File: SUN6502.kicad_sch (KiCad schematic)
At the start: 52 parts, among them J1 Barrel_Jack_MountingPin, J2 6-5530843-5, J3 6-5530843-5, J4 DE9_Socket, SW1 RESET, SW2 Power Switch, U1 W65C02SxP, U10 MAX232, U11 74LS00, U2 KM62256CLP, U3 28C256, U4 W65C22NxP, U5 74LS139, U6 74LS21, U7 W65C22NxP, U8 W65C51NxP, U9 74LS138, Y1 1Mhz, Y2 1.8432Mhz

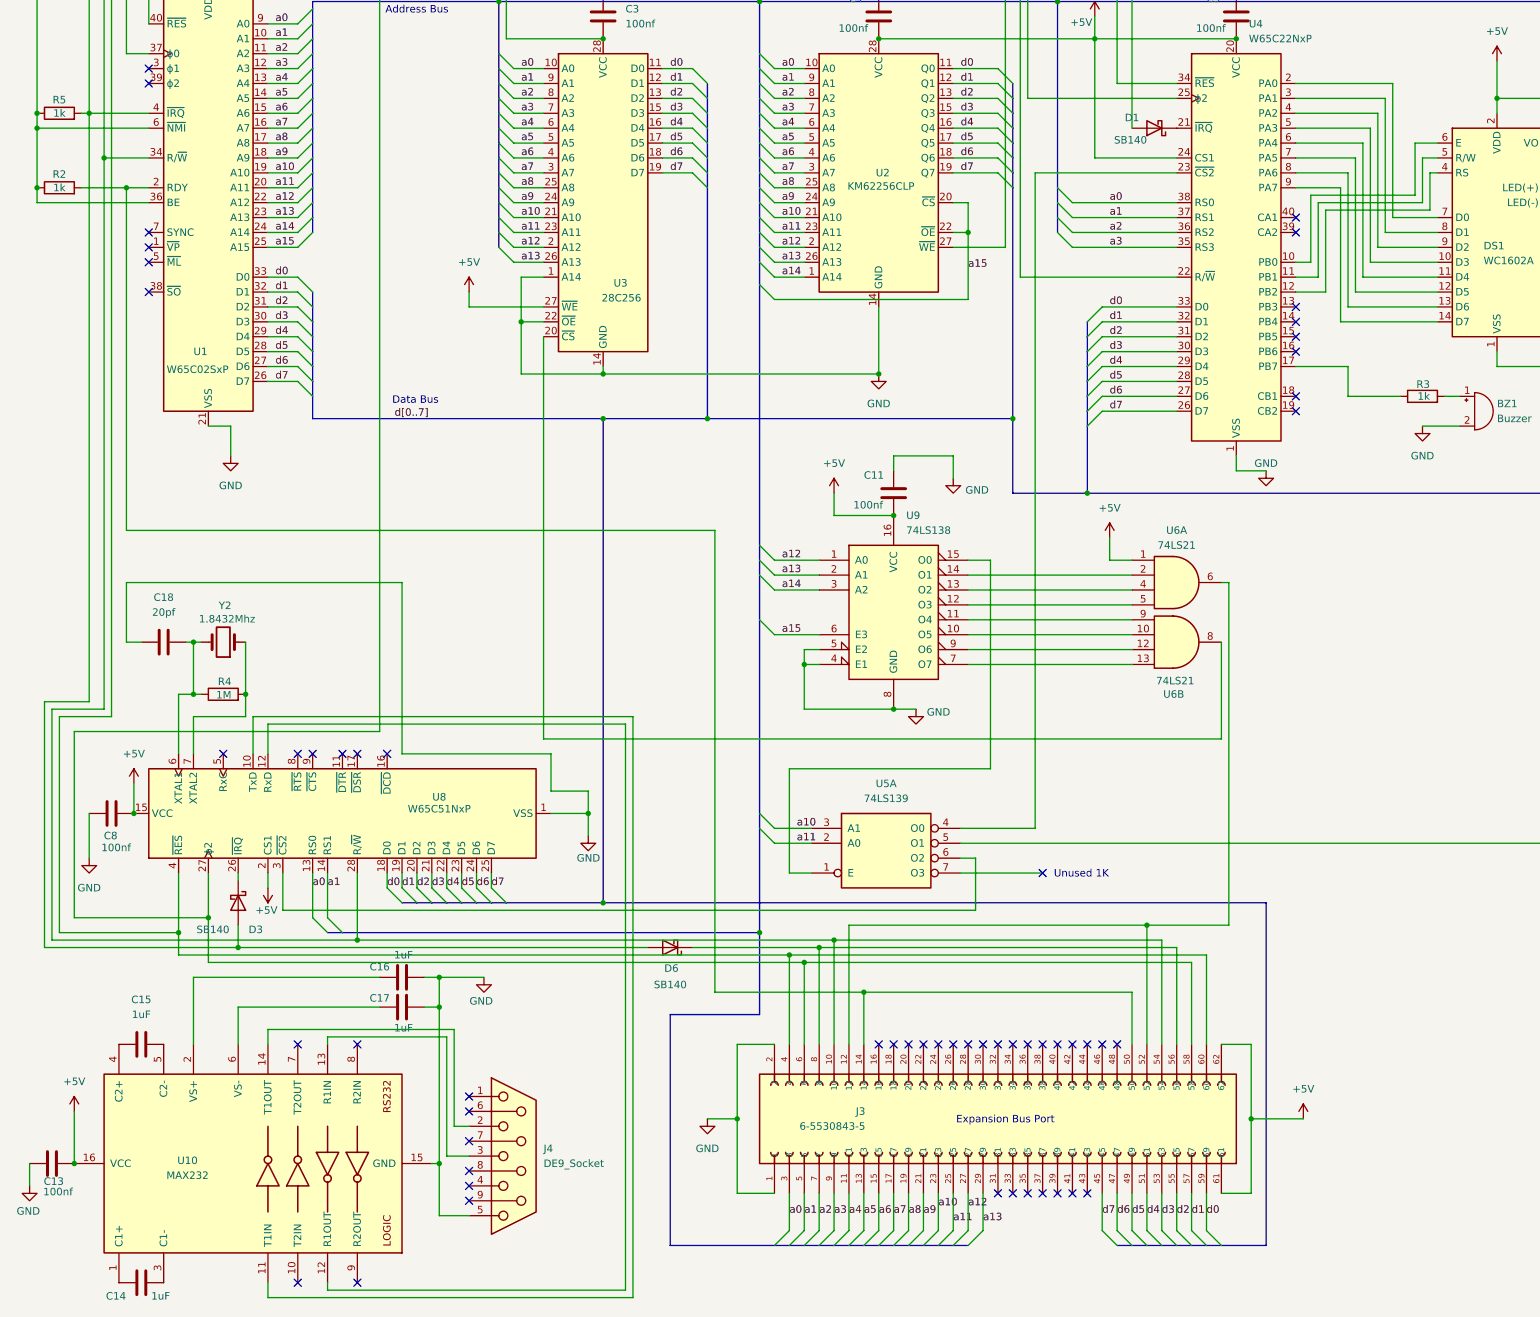
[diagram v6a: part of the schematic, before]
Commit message: pcb changed to 2 layers, CTR Added
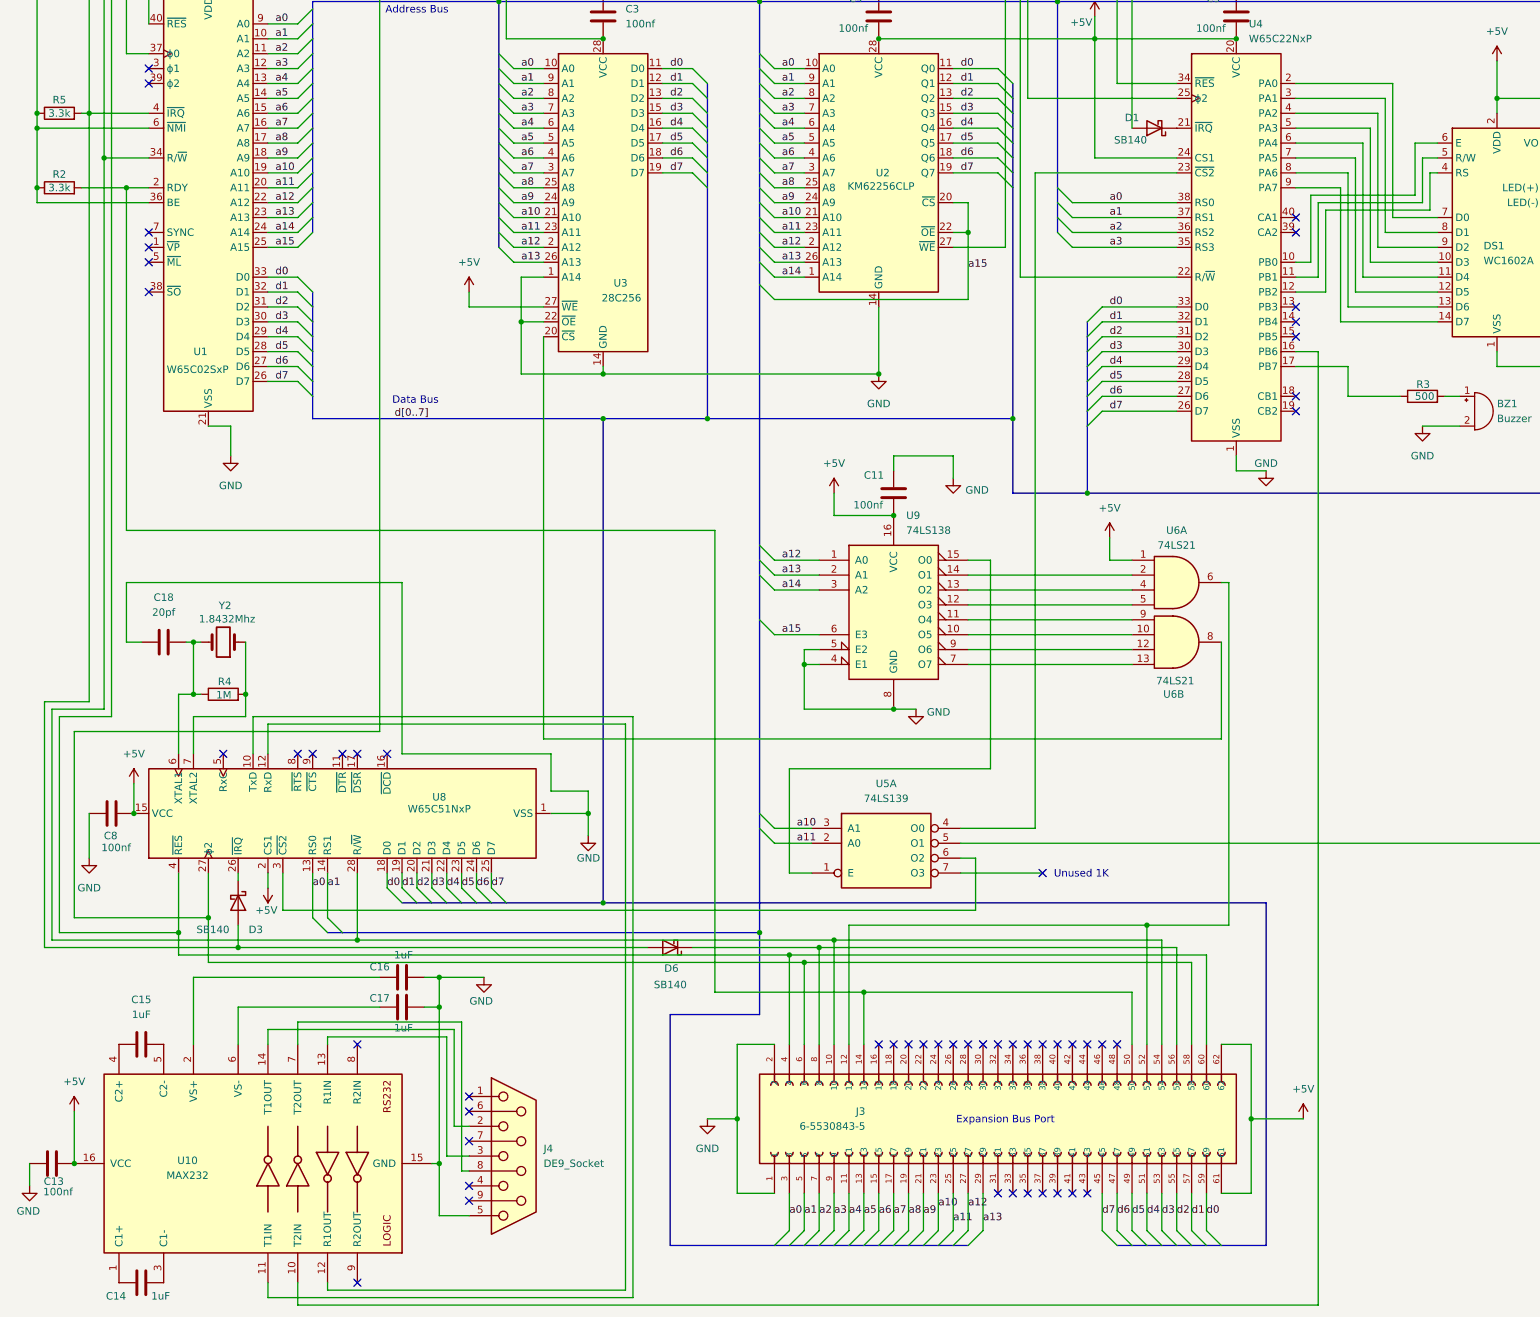
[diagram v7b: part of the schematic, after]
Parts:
- R2, R5: value 1k -> 3.3k
- R3: value 1k -> 500
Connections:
- net at J4.8: now also U10.7 (T2OUT)
- net at U10.10 (T2IN): now also U4.16 (PB6)
- no-connect marks 107 -> 103
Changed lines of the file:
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@@
 	)
 	(no_connect
-		(at 60.96 280.67)
-	)
-	(no_connect
 		(at 388.62 173.99)
 	)
@@
 	)
 	(no_connect
-		(at 231.14 121.92)
-	)
-	(no_connect
 		(at 200.66 240.03)
 	)
@@
 	)
 	(no_connect
-		(at 60.96 240.03)
-	)
-	(no_connect
 		(at 76.2 190.5)
 	)
@@
 	)
 	(no_connect
-		(at 90.17 261.62)
-	)
-	(no_connect
 		(at 363.22 209.55)
 	)
@@
 	(wire
 		(pts
+			(xy 234.95 284.48) (xy 60.96 284.48)
+		)
+		(stroke
+			(width 0)
+			(type default)
+		)
+	)
+	(wire
+		(pts
 			(xy 147.32 172.72) (xy 147.32 175.26)
 		)
@@
 	(wire
 		(pts
+			(xy 60.96 236.22) (xy 60.96 240.03)
+		)
+		(stroke
+			(width 0)
+			(type default)
+		)
+	)
+	(wire
+		(pts
 			(xy 55.88 114.3) (xy 60.96 114.3)
 		)
@@
 	(wire
 		(pts
+			(xy 234.95 121.92) (xy 234.95 284.48)
+		)
+		(stroke
+			(width 0)
+			(type default)
+		)
+	)
+	(wire
+		(pts
 			(xy 363.22 237.49) (xy 363.22 243.84)
 		)
@@
 	(wire
 		(pts
+			(xy 88.9 236.22) (xy 60.96 236.22)
+		)
+		(stroke
+			(width 0)
+			(type default)
+		)
+	)
+	(wire
+		(pts
 			(xy 55.88 101.6) (xy 60.96 101.6)
 		)
@@
 	(wire
 		(pts
+			(xy 90.17 261.62) (xy 88.9 261.62)
+		)
+		(stroke
+			(width 0)
+			(type default)
+		)
+	)
+	(wire
+		(pts
 			(xy 110.49 200.66) (xy 110.49 196.85)
 		)
@@
 	(wire
 		(pts
+			(xy 60.96 284.48) (xy 60.96 280.67)
+		)
+		(stroke
+			(width 0)
+			(type default)
+		)
+	)
+	(wire
+		(pts
 			(xy 144.78 193.04) (xy 144.78 210.82)
 		)
@@
 	(wire
 		(pts
+			(xy 88.9 261.62) (xy 88.9 236.22)
+		)
+		(stroke
+			(width 0)
+			(type default)
+		)
+	)
+	(wire
+		(pts
 			(xy 353.06 100.33) (xy 353.06 176.53)
 		)
@@
 	(wire
 		(pts
+			(xy 231.14 121.92) (xy 234.95 121.92)
+		)
+		(stroke
+			(width 0)
+			(type default)
+		)
+	)
+	(wire
+		(pts
 			(xy 43.18 190.5) (xy 43.18 184.15)
 		)
@@
 			)
 		)
-		(property "Value" "1k"
+		(property "Value" "3.3k"
 			(at 20.32 81.28 90)
 			(effects
@@
 			)
 		)
-		(property "Value" "1k"
-			(at 254 129.54 90)
+		(property "Value" "500"
+			(at 254.762 129.54 90)
 			(effects
 				(font
@@
 			)
 		)
-		(property "Value" "1k"
+		(property "Value" "3.3k"
 			(at 20.32 93.98 90)
 			(effects

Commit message: small changes
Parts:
- C18: footprint Capacitor_THT:C_Disc_D5.0mm_W2.5mm_P2.50mm -> Capacitor_THT:C_Disc_D5.0mm_W2.5mm_P5.00mm
- R4: footprint Resistor_THT:R_Axial_DIN0309_L9.0mm_D3.2mm_P20.32mm_Horizontal -> Resistor_THT:R_Axial_DIN0207_L6.3mm_D2.5mm_P15.24mm_Horizontal
- Y2: footprint Crystal:Crystal_HC18-U_Vertical -> Crystal:Crystal_HC49-U_Vertical
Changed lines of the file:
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@@
 			)
 		)
-		(property "Footprint" "Capacitor_THT:C_Disc_D5.0mm_W2.5mm_P2.50mm"
+		(property "Footprint" "Capacitor_THT:C_Disc_D5.0mm_W2.5mm_P5.00mm"
 			(at 41.91 170.4848 0)
 			(effects
@@
 			)
 		)
-		(property "Footprint" "Resistor_THT:R_Axial_DIN0309_L9.0mm_D3.2mm_P20.32mm_Horizontal"
+		(property "Footprint" "Resistor_THT:R_Axial_DIN0207_L6.3mm_D2.5mm_P15.24mm_Horizontal"
 			(at 48.26 182.118 90)
 			(effects
@@
 			)
 		)
-		(property "Footprint" "Crystal:Crystal_HC18-U_Vertical"
+		(property "Footprint" "Crystal:Crystal_HC49-U_Vertical"
 			(at 48.26 171.45 0)
 			(effects
